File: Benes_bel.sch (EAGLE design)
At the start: 26 parts, among them J1 DCJ0202, K1 HE751, K2 HE751, K3 HE751, K4 HE751, T1 BC337, T2 BC337, T3 BC337, T4 BC337, X5 FH12-08S-1SH

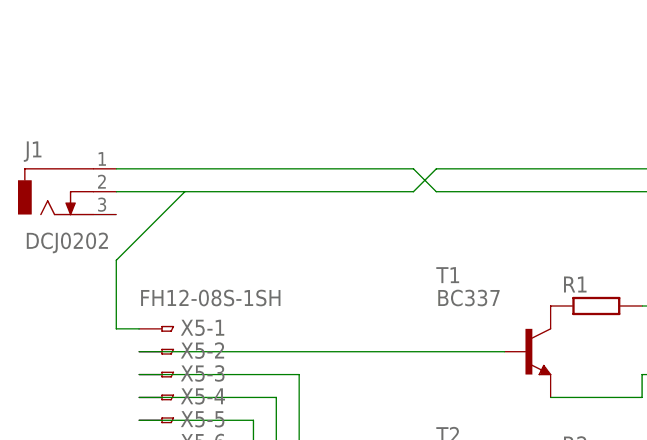
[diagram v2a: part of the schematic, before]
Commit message: correctie bord: groter gaten vr DC Jack toevoeging van vcc naar display leds meer ruimte
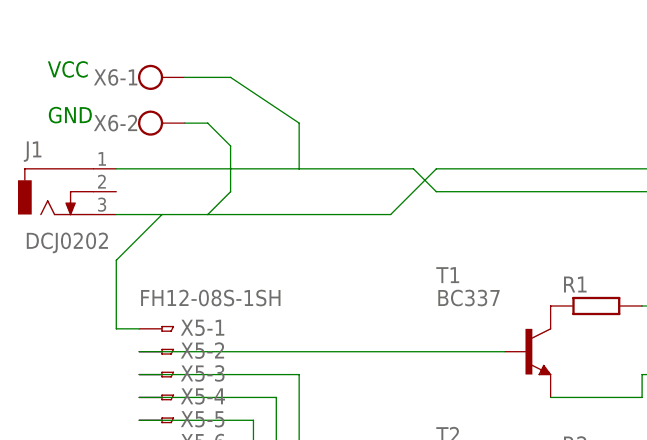
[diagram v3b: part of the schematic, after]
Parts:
- added X6: (no value), con-wago-500:W237-102
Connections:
- net N$21: now also J1.3, X6-2.KL; no longer J1.2
- net N$6: now also X6-1.KL
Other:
- note added: "GND"
- note added: "VCC"
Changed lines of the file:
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@@
 <grid distance="0.1" unitdist="inch" unit="inch" style="lines" multiple="1" display="no" altdistance="0.01" altunitdist="inch" altunit="inch"/>
 <layers>
-<layer number="1" name="Top" color="4" fill="1" visible="no" active="no"/>
-<layer number="16" name="Bottom" color="1" fill="1" visible="no" active="no"/>
-<layer number="17" name="Pads" color="2" fill="1" visible="no" active="no"/>
-<layer number="18" name="Vias" color="2" fill="1" visible="no" active="no"/>
-<layer number="19" name="Unrouted" color="6" fill="1" visible="no" active="no"/>
-<layer number="20" name="Dimension" color="15" fill="1" visible="no" active="no"/>
-<layer number="21" name="tPlace" color="7" fill="1" visible="no" active="no"/>
-<layer number="22" name="bPlace" color="7" fill="1" visible="no" active="no"/>
-<layer number="23" name="tOrigins" color="15" fill="1" visible="no" active="no"/>
-<layer number="24" name="bOrigins" color="15" fill="1" visible="no" active="no"/>
-<layer number="25" name="tNames" color="7" fill="1" visible="no" active="no"/>
-<layer number="26" name="bNames" color="7" fill="1" visible="no" active="no"/>
-<layer number="27" name="tValues" color="7" fill="1" visible="no" active="no"/>
-<layer number="28" name="bValues" color="7" fill="1" visible="no" active="no"/>
+<layer number="1" name="Top" color="4" fill="1" visible="yes" active="no"/>
+<layer number="16" name="Bottom" color="1" fill="1" visible="yes" active="no"/>
+<layer number="17" name="Pads" color="2" fill="1" visible="yes" active="no"/>
+<layer number="18" name="Vias" color="2" fill="1" visible="yes" active="no"/>
+<layer number="19" name="Unrouted" color="6" fill="1" visible="yes" active="no"/>
+<layer number="20" name="Dimension" color="15" fill="1" visible="yes" active="no"/>
+<layer number="21" name="tPlace" color="7" fill="1" visible="yes" active="no"/>
+<layer number="22" name="bPlace" color="7" fill="1" visible="yes" active="no"/>
+<layer number="23" name="tOrigins" color="15" fill="1" visible="yes" active="no"/>
+<layer number="24" name="bOrigins" color="15" fill="1" visible="yes" active="no"/>
+<layer number="25" name="tNames" color="7" fill="1" visible="yes" active="no"/>
+<layer number="26" name="bNames" color="7" fill="1" visible="yes" active="no"/>
+<layer number="27" name="tValues" color="7" fill="1" visible="yes" active="no"/>
+<layer number="28" name="bValues" color="7" fill="1" visible="yes" active="no"/>
 <layer number="29" name="tStop" color="7" fill="3" visible="no" active="no"/>
 <layer number="30" name="bStop" color="7" fill="6" visible="no" active="no"/>
@@
 <layer number="35" name="tGlue" color="7" fill="4" visible="no" active="no"/>
 <layer number="36" name="bGlue" color="7" fill="5" visible="no" active="no"/>
-<layer number="37" name="tTest" color="7" fill="1" visible="no" active="no"/>
-<layer number="38" name="bTest" color="7" fill="1" visible="no" active="no"/>
+<layer number="37" name="tTest" color="7" fill="1" visible="yes" active="no"/>
+<layer number="38" name="bTest" color="7" fill="1" visible="yes" active="no"/>
 <layer number="39" name="tKeepout" color="4" fill="11" visible="no" active="no"/>
 <layer number="40" name="bKeepout" color="1" fill="11" visible="no" active="no"/>
@@
 <layer number="44" name="Drills" color="7" fill="1" visible="no" active="no"/>
 <layer number="45" name="Holes" color="7" fill="1" visible="no" active="no"/>
-<layer number="46" name="Milling" color="3" fill="1" visible="no" active="no"/>
-<layer number="47" name="Measures" color="7" fill="1" visible="no" active="no"/>
-<layer number="48" name="Document" color="7" fill="1" visible="no" active="no"/>
-<layer number="49" name="Reference" color="7" fill="1" visible="no" active="no"/>
-<layer number="51" name="tDocu" color="6" fill="1" visible="no" active="no"/>
-<layer number="52" name="bDocu" color="7" fill="1" visible="no" active="no"/>
+<layer number="46" name="Milling" color="3" fill="1" visible="yes" active="no"/>
+<layer number="47" name="Measures" color="7" fill="1" visible="yes" active="no"/>
+<layer number="48" name="Document" color="7" fill="1" visible="yes" active="no"/>
+<layer number="49" name="Reference" color="7" fill="1" visible="yes" active="no"/>
+<layer number="51" name="tDocu" color="7" fill="1" visible="yes" active="no"/>
+<layer number="52" name="bDocu" color="7" fill="1" visible="yes" active="no"/>
 <layer number="90" name="Modules" color="5" fill="1" visible="yes" active="yes"/>
 <layer number="91" name="Nets" color="2" fill="1" visible="yes" active="yes"/>
@@
 <part name="D4" library="led" deviceset="U57X32" device=""/>
 <part name="R8" library="resistor" deviceset="R-EU_" device="0207/12" value="330k"/>
+<part name="X6" library="con-wago-500" deviceset="W237-102" device=""/>
 </parts>
 <sheets>
 <sheet>
 <plain>
+<text x="-2.54" y="119.38" size="1.778" layer="91">GND</text>
+<text x="-2.54" y="124.46" size="1.778" layer="91">VCC</text>
 </plain>
 <instances>
@@
 <instance part="D4" gate="1" x="96.52" y="101.6" rot="R90"/>
 <instance part="R8" gate="G$1" x="88.9" y="109.22"/>
+<instance part="X6" gate="-1" x="7.62" y="124.46"/>
+<instance part="X6" gate="-2" x="7.62" y="119.38"/>
 </instances>
 <busses>
@@
 <wire x1="66.04" y1="50.8" x2="63.5" y2="50.8" width="0.1524" layer="91"/>
 <pinref part="J1" gate="G$1" pin="1"/>
-<wire x1="5.08" y1="114.3" x2="38.1" y2="114.3" width="0.1524" layer="91"/>
+<wire x1="5.08" y1="114.3" x2="25.4" y2="114.3" width="0.1524" layer="91"/>
+<wire x1="25.4" y1="114.3" x2="38.1" y2="114.3" width="0.1524" layer="91"/>
 <wire x1="38.1" y1="114.3" x2="40.64" y2="111.76" width="0.1524" layer="91"/>
 <wire x1="40.64" y1="111.76" x2="66.04" y2="111.76" width="0.1524" layer="91"/>
+<pinref part="X6" gate="-1" pin="KL"/>
+<wire x1="12.7" y1="124.46" x2="17.78" y2="124.46" width="0.1524" layer="91"/>
+<wire x1="17.78" y1="124.46" x2="25.4" y2="119.38" width="0.1524" layer="91"/>
+<wire x1="25.4" y1="119.38" x2="25.4" y2="114.3" width="0.1524" layer="91"/>
 </segment>
 </net>
@@
 <wire x1="81.28" y1="114.3" x2="40.64" y2="114.3" width="0.1524" layer="91"/>
 <wire x1="101.6" y1="93.98" x2="81.28" y2="93.98" width="0.1524" layer="91"/>
-<wire x1="38.1" y1="111.76" x2="40.64" y2="114.3" width="0.1524" layer="91"/>
-<pinref part="J1" gate="G$1" pin="2"/>
-<wire x1="5.08" y1="111.76" x2="12.7" y2="111.76" width="0.1524" layer="91"/>
-<wire x1="38.1" y1="111.76" x2="12.7" y2="111.76" width="0.1524" layer="91"/>
-<wire x1="12.7" y1="111.76" x2="5.08" y2="104.14" width="0.1524" layer="91"/>
+<wire x1="35.56" y1="109.22" x2="40.64" y2="114.3" width="0.1524" layer="91"/>
+<wire x1="35.56" y1="109.22" x2="15.24" y2="109.22" width="0.1524" layer="91"/>
+<wire x1="15.24" y1="109.22" x2="10.16" y2="109.22" width="0.1524" layer="91"/>
+<wire x1="10.16" y1="109.22" x2="5.08" y2="104.14" width="0.1524" layer="91"/>
 <pinref part="X5" gate="-1" pin="1"/>
 <wire x1="7.62" y1="96.52" x2="5.08" y2="96.52" width="0.1524" layer="91"/>
 <wire x1="5.08" y1="96.52" x2="5.08" y2="104.14" width="0.1524" layer="91"/>
-</segment>
-</net>
+<pinref part="J1" gate="G$1" pin="3"/>
+<wire x1="5.08" y1="109.22" x2="10.16" y2="109.22" width="0.1524" layer="91"/>
+<wire x1="15.24" y1="109.22" x2="17.78" y2="111.76" width="0.1524" layer="91"/>
+<wire x1="17.78" y1="111.76" x2="17.78" y2="116.84" width="0.1524" layer="91"/>
+<pinref part="X6" gate="-2" pin="KL"/>
+<wire x1="17.78" y1="116.84" x2="15.24" y2="119.38" width="0.1524" layer="91"/>
+<wire x1="15.24" y1="119.38" x2="12.7" y2="119.38" width="0.1524" layer="91"/>
+</segment>
+</net>

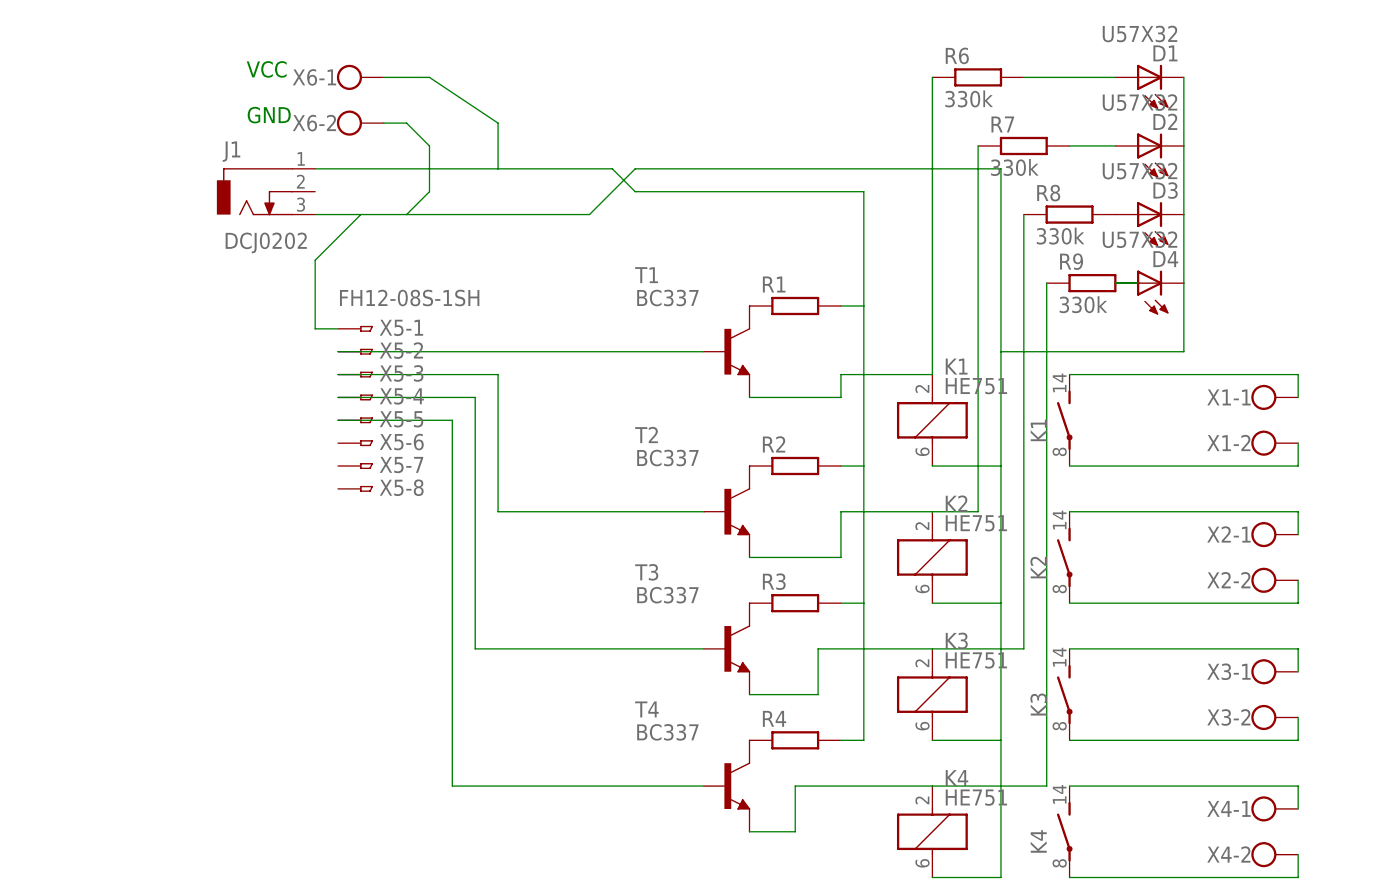
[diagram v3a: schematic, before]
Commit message: met high level switch + speaker + mic
eerste versie was met een low level switch
nu met met darlington (npn+pnp)
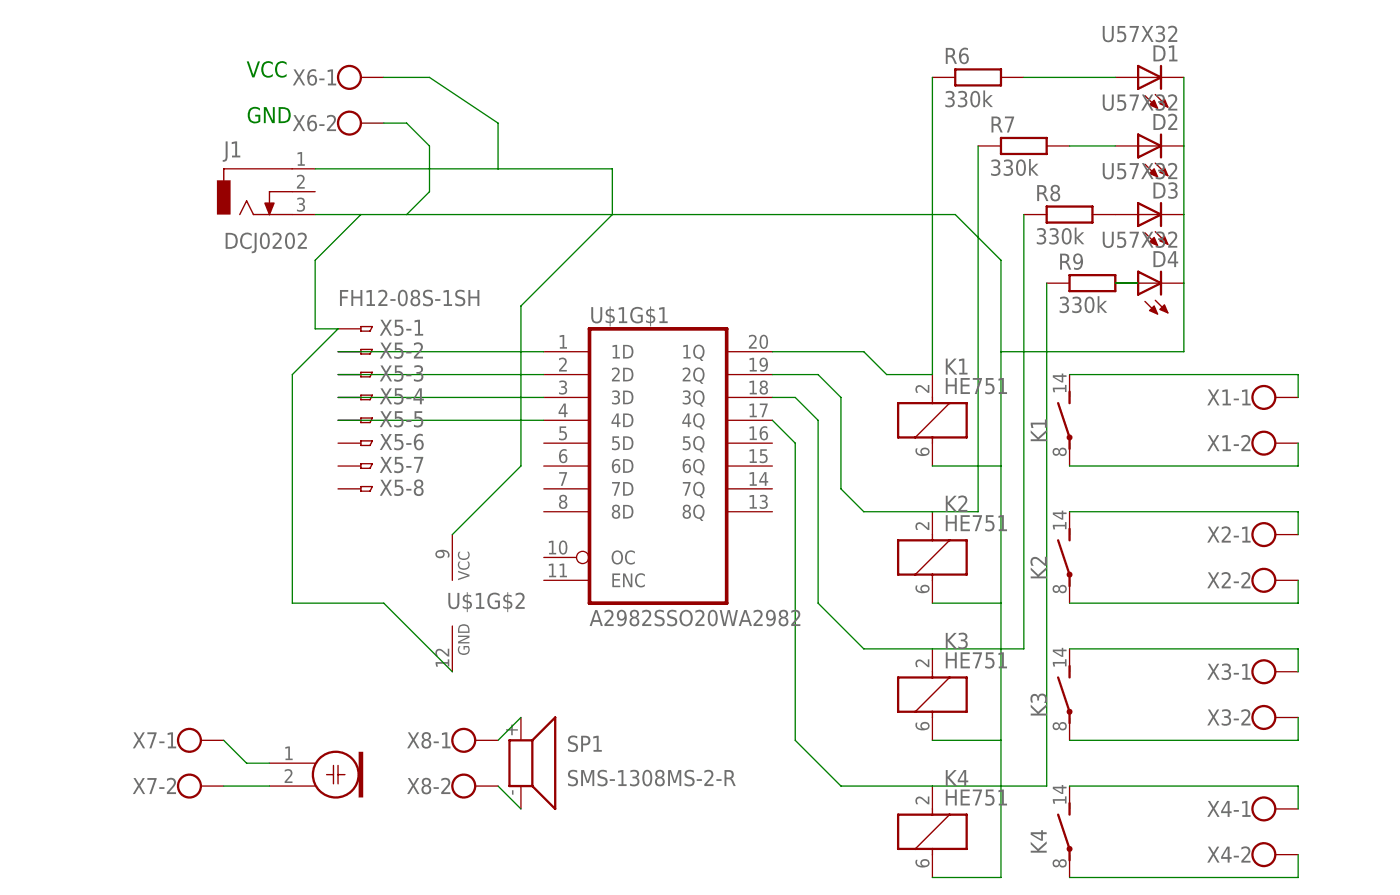
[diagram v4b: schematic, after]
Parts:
- removed R1, R2, R3, R4: (no value), resistor:R-EU_0207/12
- removed T1, T2, T3, T4: BC337, transistor:BC337
- added M1: ELECTRET_MICROPHON-WM-61B, microphon:ELECTRET_MICROPHON-WM-61B
- added SP1: SMS-1308MS-2-R, speaker:SMS-1308MS-2-R
- added U$1: A2982SSO20WA2982, gxb:A2982SSO20WA2982
- added X7, X8: (no value), con-wago-500:W237-102
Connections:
- removed net N$10: T4.B, X5-5.1
- new net N$22: J1.1, U$1G$2.VCC, X6-1.KL
- net N$1: now also U$1G$1.1D, X5-2.1; no longer R1.1, T1.C
- net N$19: now also U$1G$1.3Q; no longer T3.E
- net N$2: now also U$1G$1.2D, X5-3.1; no longer R2.1, T2.C
- net N$20: now also U$1G$1.4Q; no longer T4.E
- net N$21: now also U$1G$2.GND
- net N$23: now also U$1G$1.1Q; no longer T1.E
- net N$3: now also U$1G$1.3D, X5-4.1; no longer R3.1, T3.C
- net N$4: now also U$1G$1.4D, X5-5.1; no longer R4.1, T4.C
- net N$5: now also U$1G$1.2Q; no longer T2.E
- net N$6: now also SP1.1, X8-1.KL; no longer J1.1, R1.2, R2.2, R3.2, R4.2, X6-1.KL
- net N$7: now also SP1.2, X8-2.KL; no longer T1.B, X5-2.1
- net N$8: now also M1.1, X7-1.KL; no longer T2.B, X5-3.1
- net N$9: now also M1.2, X7-2.KL; no longer T3.B, X5-4.1
